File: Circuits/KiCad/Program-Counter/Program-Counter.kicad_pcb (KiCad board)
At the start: 2 copper layers, 13 parts, among them J1 Conn_01x17_Male, J2 MAR_BUS_OUT, U1 7402, U2 74LS191, U3 74LS191, U4 74LS191, U5 74LS191, U6 74LS245, U7 74LS245

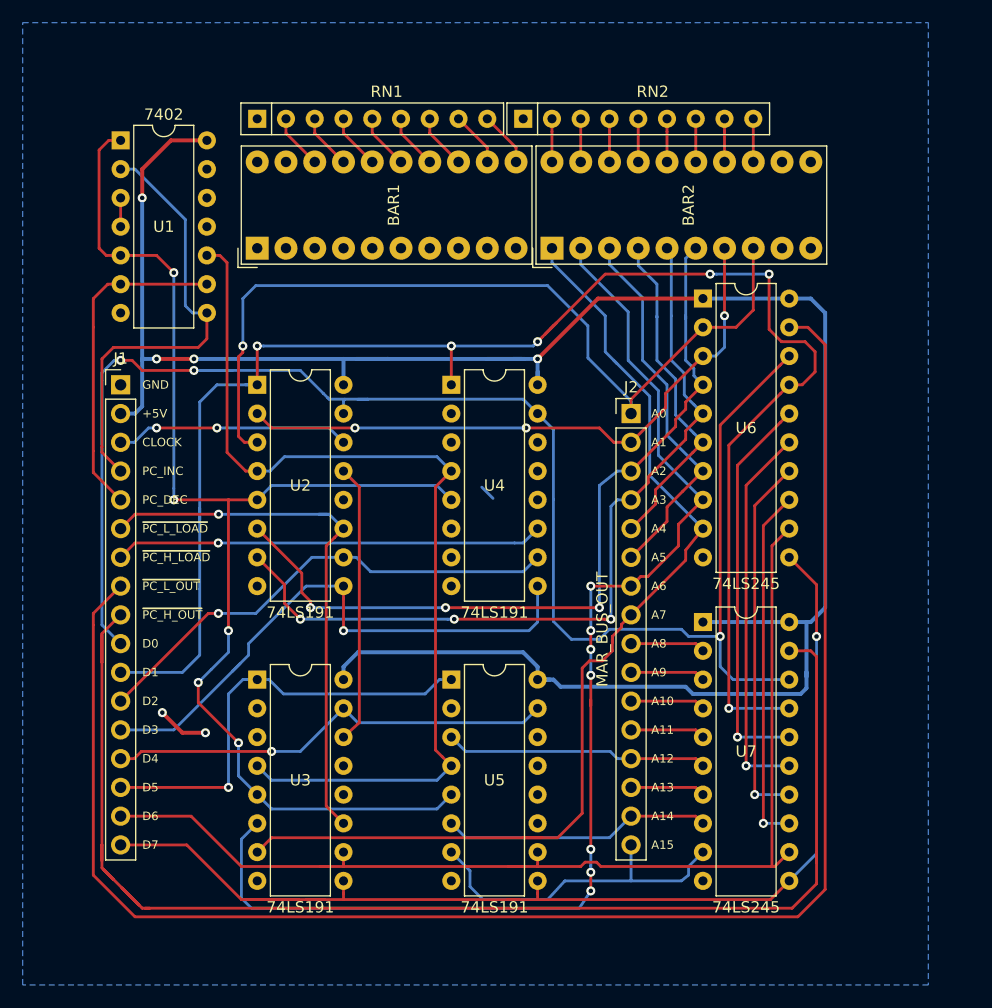
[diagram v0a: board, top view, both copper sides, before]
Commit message: Finished Program Counter schematic & PCB
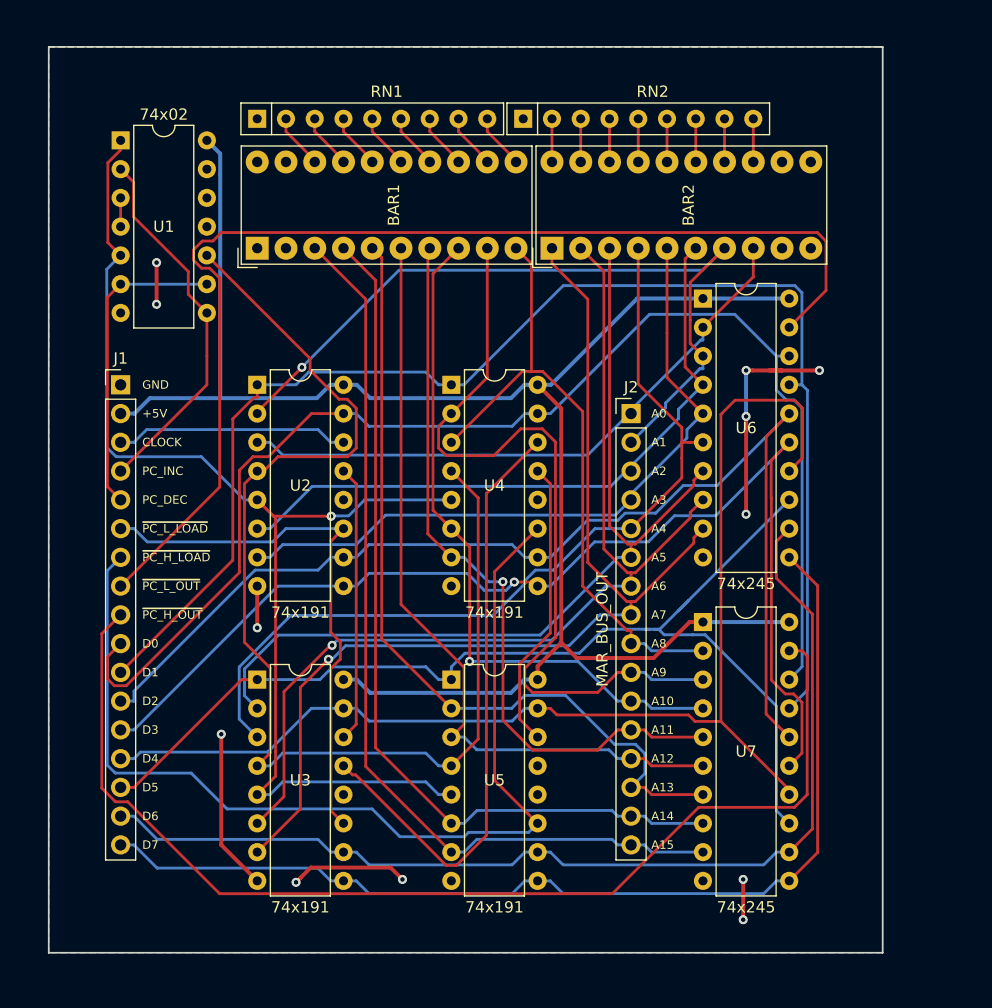
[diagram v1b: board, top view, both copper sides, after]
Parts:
- U1: value 7402 -> 74x02
- U2, U3, U4, U5: value 74LS191 -> 74x191
- U6, U7: value 74LS245 -> 74x245
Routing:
- net Net-(BAR1-Pad5): track 6.61 -> 73.3 mm
- net Net-(BAR1-Pad9): track 6.61 -> 71.1 mm
- net Net-(BAR1-Pad7): track 6.61 -> 65.7 mm, vias 0 -> 1
- net Net-(BAR1-Pad8): track 6.61 -> 61.1 mm, vias 0 -> 1
- net Net-(BAR1-Pad4): track 23.8 -> 77.9 mm
- net Net-(U3-Pad13): track 0.00 -> 54.0 mm
- net Net-(BAR1-Pad3): track 30.1 -> 81.5 mm
- net GND: track 4.55 -> 55.9 mm, vias 2 -> 12
- net ~PC_H_LOAD: track 37.9 -> 89.1 mm, vias 1 -> 0
- net Net-(BAR1-Pad10): track 6.61 -> 56.9 mm
- net Net-(BAR2-Pad4): track 29.9 -> 76.8 mm
- net Net-(BAR2-Pad3): track 33.4 -> 79.7 mm
- net Net-(BAR1-Pad6): track 23.3 -> 69.2 mm
- net ~PC_L_OUT: track 145.6 -> 100.5 mm
- net +5V: track 195.2 -> 155.4 mm, vias 4 -> 0
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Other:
- board outline added: 73.7 x 80 mm

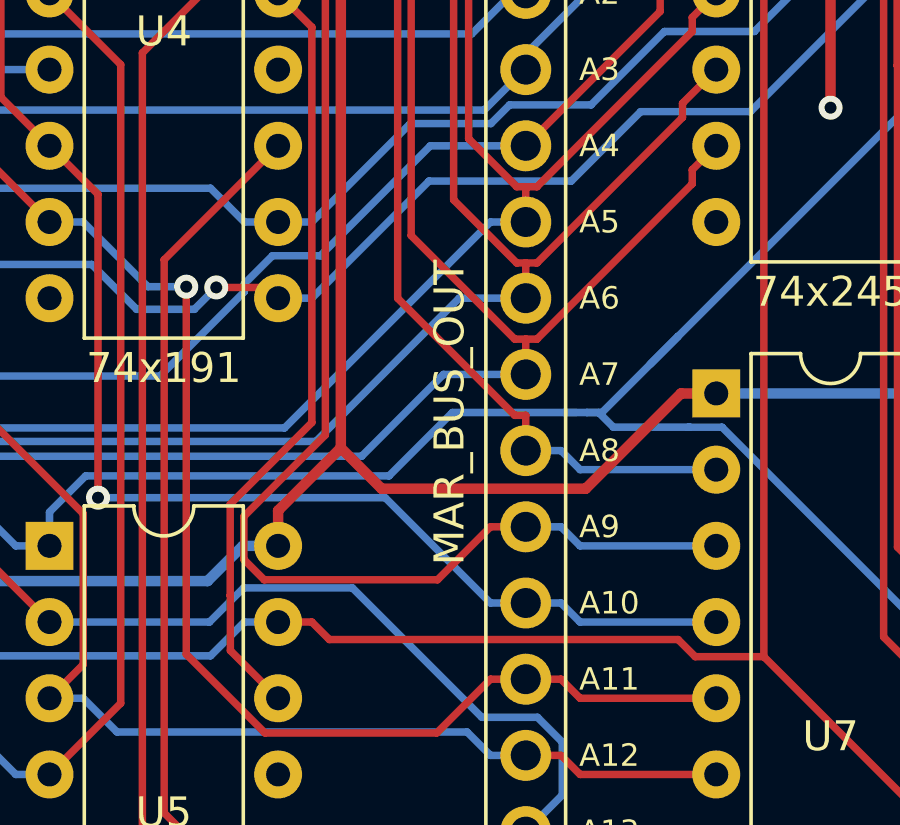
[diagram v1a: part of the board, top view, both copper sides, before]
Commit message: Added Stack Pointer schematics & PCB. Rerouted Clock based autorouter output
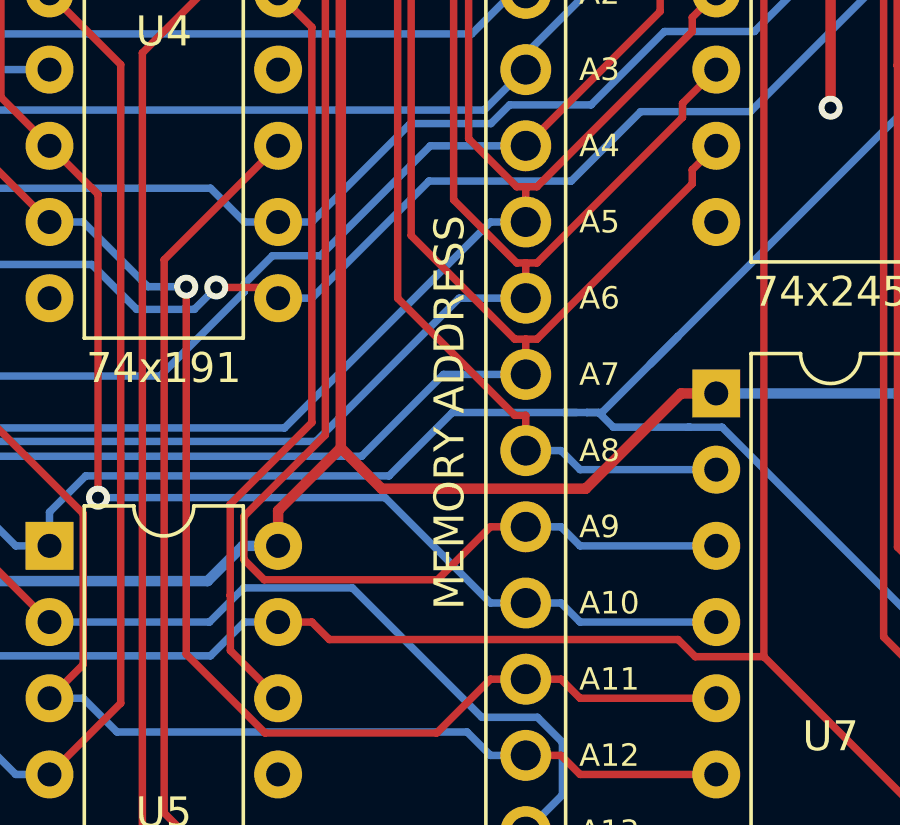
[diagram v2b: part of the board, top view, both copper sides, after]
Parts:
- J2: value MAR_BUS_OUT -> MEMORY ADDRESS
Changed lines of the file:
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@@
     (pcbplotparams
       (layerselection 0x010fc_ffffffff)
-      (usegerberextensions false)
+      (usegerberextensions true)
       (usegerberattributes false)
       (usegerberadvancedattributes false)
@@
       (outputformat 1)
       (mirror false)
-      (drillshape 1)
+      (drillshape 0)
       (scaleselection 1)
-      (outputdirectory ""))
+      (outputdirectory "gerber"))
   )
   (net 0 "")
@@
       (effects (font (size 1 1) (thickness 0.15)))
     )
-    (fp_text value MAR_BUS_OUT (at -2.54 19.05 90) (layer F.SilkS)
-      (effects (font (size 1 1) (thickness 0.15)))
-    )
+    (fp_text value "MEMORY ADDRESS" (at -2.54 19.05 90) (layer F.SilkS)
+      (effects (font (size 1 1) (thickness 0.15)))
+    )

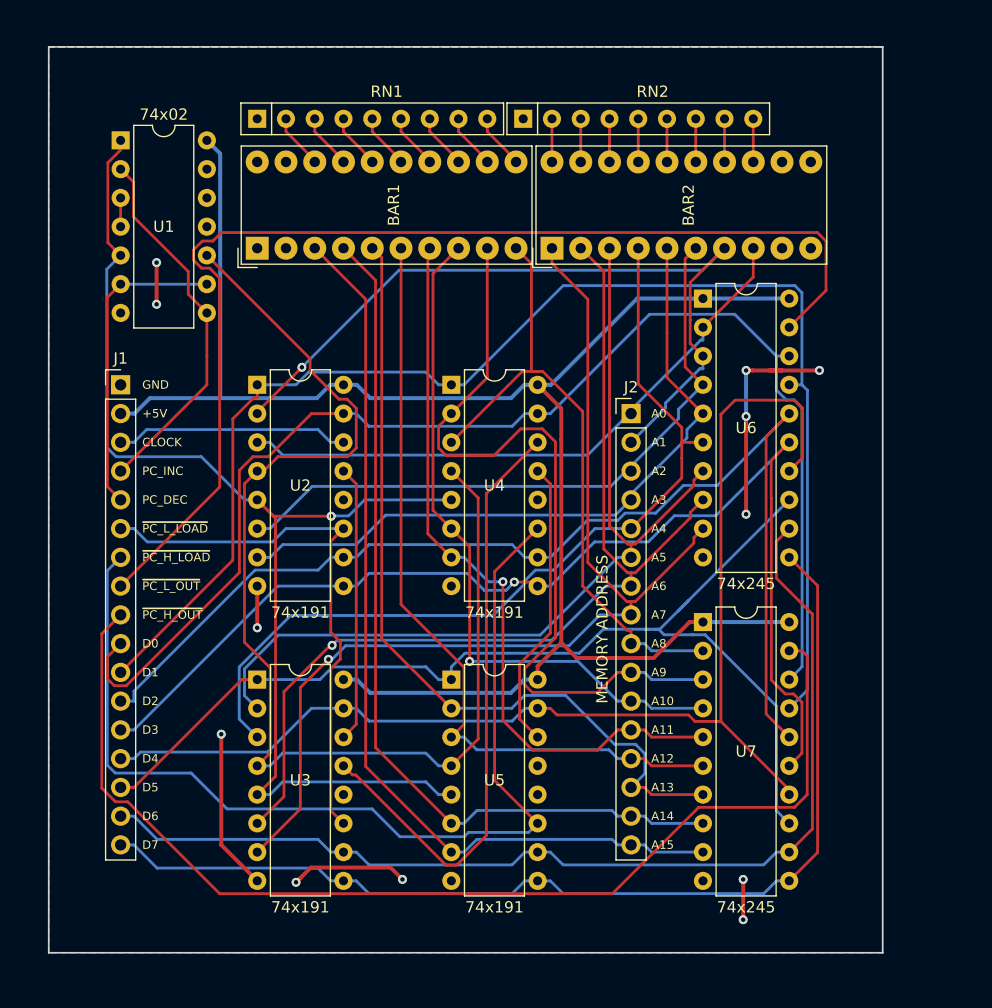
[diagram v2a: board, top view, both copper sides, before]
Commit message: Made sure spacing between headers is always 2.54mm pitch
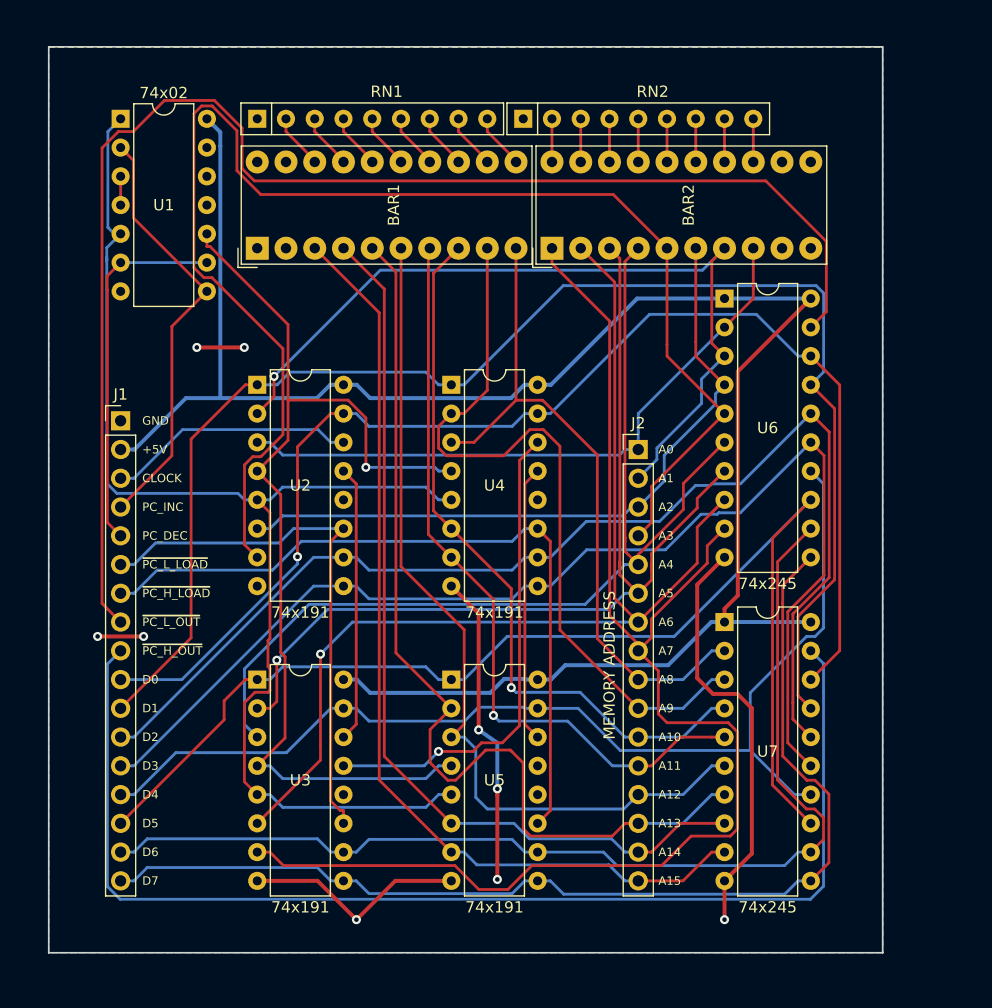
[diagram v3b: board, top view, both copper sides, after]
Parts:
- moved J2 3.24 mm to (79.4, 52.7)
- moved J1 3.17 mm to (33.7, 50.2)
- moved U6 1.91 mm to (87.0, 39.4)
- moved U7 1.91 mm to (87.0, 67.9)
- moved U1 1.90 mm to (33.7, 23.5)
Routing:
- net Net-(BAR2-Pad5): track 61.3 -> 125.2 mm
- net GND: track 55.9 -> 93.3 mm, vias 12 -> 9
- net Net-(BAR2-Pad1): track 92.8 -> 122.9 mm, vias 1 -> 0
- net ~PC_L_OUT: track 100.5 -> 123.7 mm
- net ~PC_H_LOAD: track 89.1 -> 66.2 mm
- net ~CLK_EN: track 108.4 -> 90.9 mm, vias 0 -> 1
- net +5V: track 155.4 -> 168.8 mm
- net Net-(BAR2-Pad4): track 76.8 -> 88.4 mm
- net Net-(BAR1-Pad5): track 73.3 -> 84.9 mm
- net Net-(U3-Pad13): track 54.0 -> 42.7 mm, vias 0 -> 1
- net DATA_BUS4: track 106.5 -> 96.5 mm
- net Net-(BAR2-Pad2): track 88.3 -> 97.4 mm
- net DATA_BUS5: track 97.4 -> 106.1 mm
- net Net-(BAR2-Pad3): track 79.7 -> 87.3 mm, vias 0 -> 1
- net Net-(BAR1-Pad6): track 69.2 -> 76.8 mm
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
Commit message: Updated Program Counter schematic and PCB
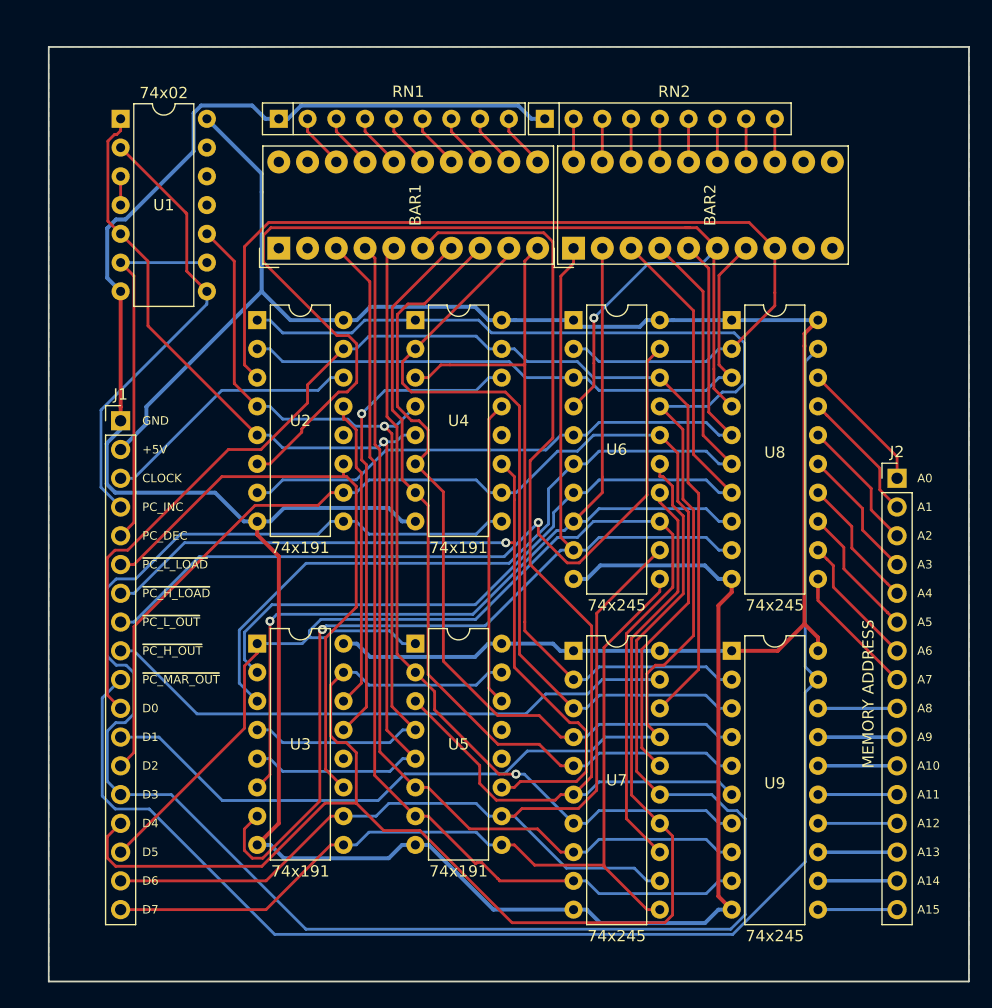
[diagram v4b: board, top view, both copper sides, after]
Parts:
- added U8: 74x245, Package_DIP:DIP-20_W7.62mm, F.Cu at (87.6, 41.3)
- added U9: 74x245, Package_DIP:DIP-20_W7.62mm, F.Cu at (87.6, 70.5)
- J1: value Conn_01x17_Male -> Conn_01x18_Male; footprint Connector_PinHeader_2.54mm:PinHeader_1x17_P2.54mm_Vertical -> Connector_PinHeader_2.54mm:PinHeader_1x18_P2.54mm_Vertical
- moved J2 23.0 mm to (102.2, 55.2)
- moved U7 13.6 mm to (73.7, 70.5)
- moved U6 13.5 mm to (73.7, 41.3)
- moved U4 6.54 mm to (59.7, 41.3)
- moved U2 5.72 mm to (45.7, 41.3)
- moved U5 4.49 mm to (59.7, 69.8)
- moved U3 3.18 mm to (45.7, 69.8)
- moved BAR1 1.91 mm to (47.6, 34.9)
- moved BAR2 1.91 mm to (73.7, 34.9)
- moved RN1 1.91 mm to (47.6, 23.5)
- moved RN2 1.91 mm to (71.1, 23.5)
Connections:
- J1 pad 10: DATA_BUS0 -> ~PC_MAR_OUT
- J1 pad 11: DATA_BUS1 -> DATA_BUS0
- J1 pad 12: DATA_BUS2 -> DATA_BUS1
- J1 pad 13: DATA_BUS3 -> DATA_BUS2
- J1 pad 14: DATA_BUS4 -> DATA_BUS3
- J1 pad 15: DATA_BUS5 -> DATA_BUS4
- J1 pad 16: DATA_BUS6 -> DATA_BUS5
- J1 pad 17: DATA_BUS7 -> DATA_BUS6
- J2 pad 1: Net-(BAR2-Pad8) -> Net-(J2-Pad1)
- J2 pad 10: Net-(BAR1-Pad9) -> Net-(J2-Pad10)
- J2 pad 11: Net-(BAR1-Pad8) -> Net-(J2-Pad11)
- J2 pad 12: Net-(BAR1-Pad7) -> Net-(J2-Pad12)
- J2 pad 13: Net-(BAR1-Pad6) -> Net-(J2-Pad13)
- J2 pad 14: Net-(BAR1-Pad5) -> Net-(J2-Pad14)
- J2 pad 15: Net-(BAR1-Pad4) -> Net-(J2-Pad15)
- J2 pad 16: Net-(BAR1-Pad3) -> Net-(J2-Pad16)
- J2 pad 2: Net-(BAR2-Pad7) -> Net-(J2-Pad2)
- J2 pad 3: Net-(BAR2-Pad6) -> Net-(J2-Pad3)
- J2 pad 4: Net-(BAR2-Pad5) -> Net-(J2-Pad4)
- J2 pad 5: Net-(BAR2-Pad4) -> Net-(J2-Pad5)
- J2 pad 6: Net-(BAR2-Pad3) -> Net-(J2-Pad6)
- J2 pad 7: Net-(BAR2-Pad2) -> Net-(J2-Pad7)
- J2 pad 8: Net-(BAR2-Pad1) -> Net-(J2-Pad8)
- J2 pad 9: Net-(BAR1-Pad10) -> Net-(J2-Pad9)
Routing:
- net GND: track 93.3 -> 221.3 mm, vias 9 -> 0
- net ~PC_MAR_OUT: track 0.00 -> 127.5 mm
- net DATA_BUS3: track 105.0 -> 170.2 mm
- net Net-(BAR2-Pad5): track 125.2 -> 63.0 mm
- net ~PC_L_OUT: track 123.7 -> 68.1 mm, vias 0 -> 1
- net ~PC_H_OUT: track 106.8 -> 51.2 mm
- net Net-(BAR2-Pad6): track 62.3 -> 107.2 mm, vias 0 -> 1
- net DATA_BUS4: track 96.5 -> 130.2 mm
- net Net-(BAR2-Pad8): track 56.3 -> 86.1 mm
- net Net-(BAR2-Pad1): track 122.9 -> 95.4 mm, vias 0 -> 1
- net Net-(BAR1-Pad6): track 76.8 -> 98.6 mm
- net DOWN_~UP: track 113.9 -> 92.9 mm, vias 0 -> 1
- net Net-(BAR2-Pad7): track 72.8 -> 56.8 mm, vias 1 -> 0
- net ~CLK_EN: track 90.9 -> 75.4 mm
- net DATA_BUS7: track 96.2 -> 80.7 mm
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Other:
- board size 73.7 x 80 mm -> 81.3 x 82.5 mm
- board text added: "~PC_MAR_OUT"
